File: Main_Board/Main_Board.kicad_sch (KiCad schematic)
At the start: 30 parts, among them J1 RJ45_LED_Shielded, SW1 SW_SPDT, SW2 SW_Push, SW3 SW_Push, SW4 SW_Push, SW5 SW_Push, SW6 SW_Push, SW7 SW_Push, SW8 SW_Push, SW9 SW_Push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

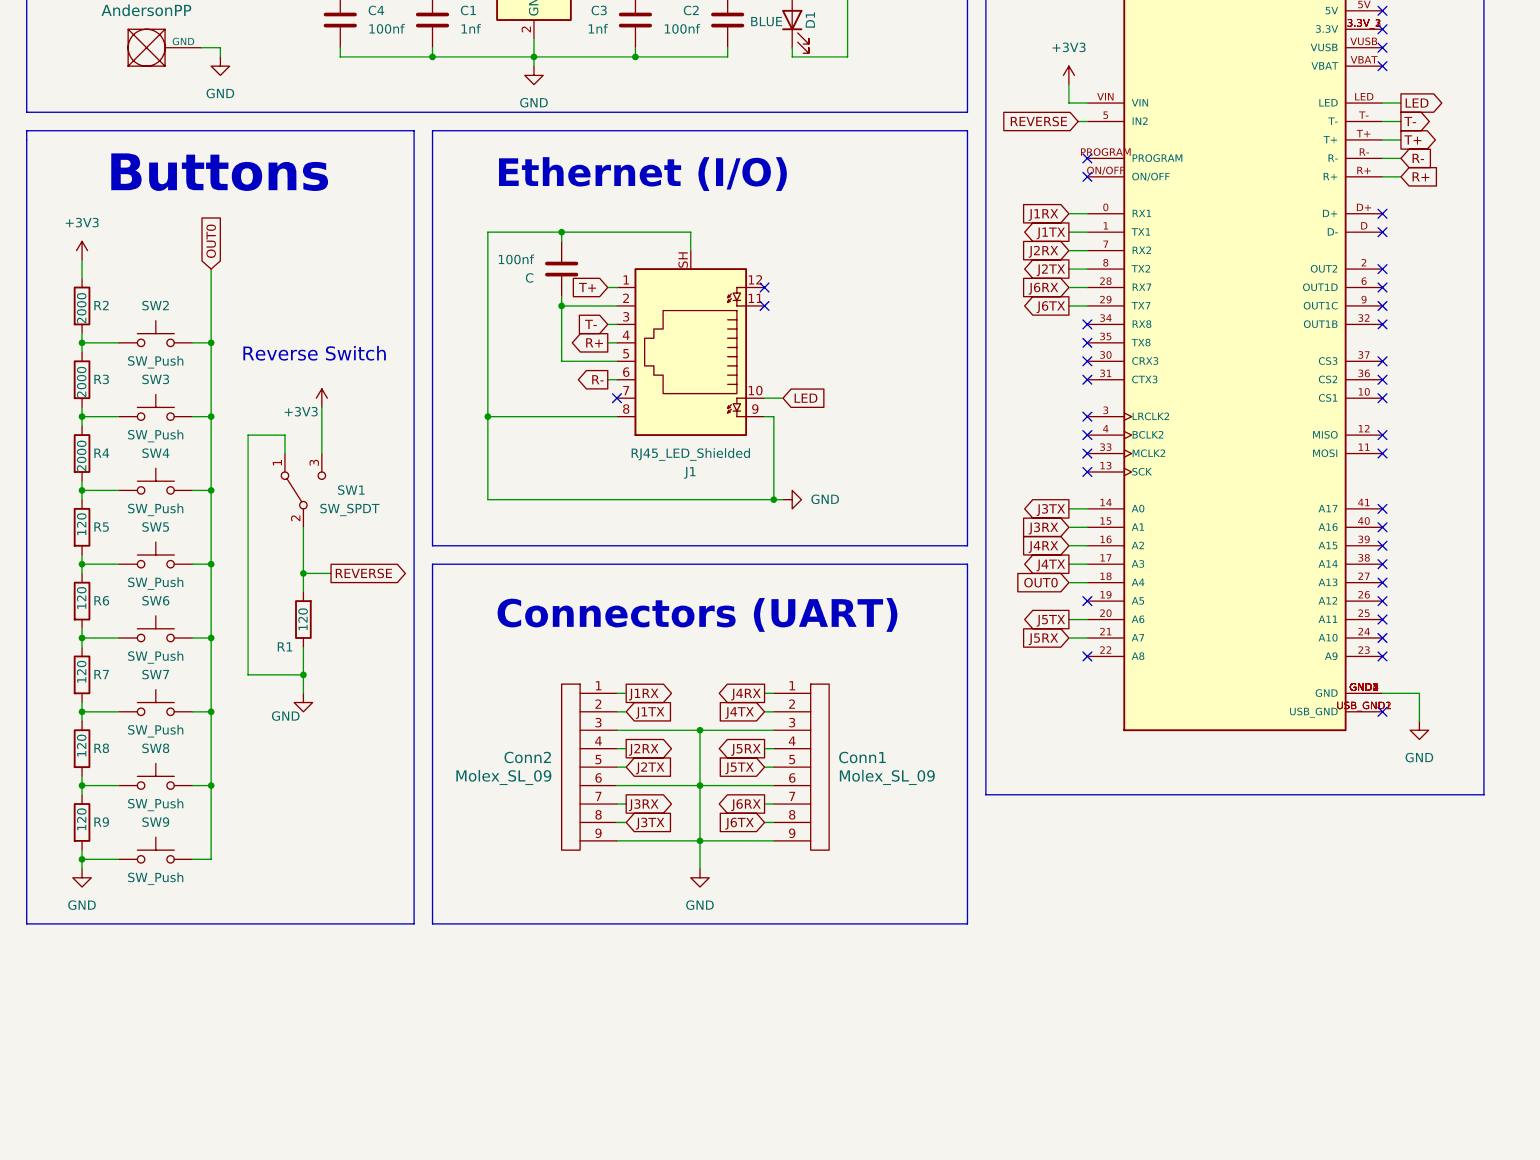
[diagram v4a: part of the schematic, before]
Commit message: Added Keyboard Matrix Layout
Added a keyboard circuit layout so any button can be pressed at the same time and programmed to work like a keyboard.
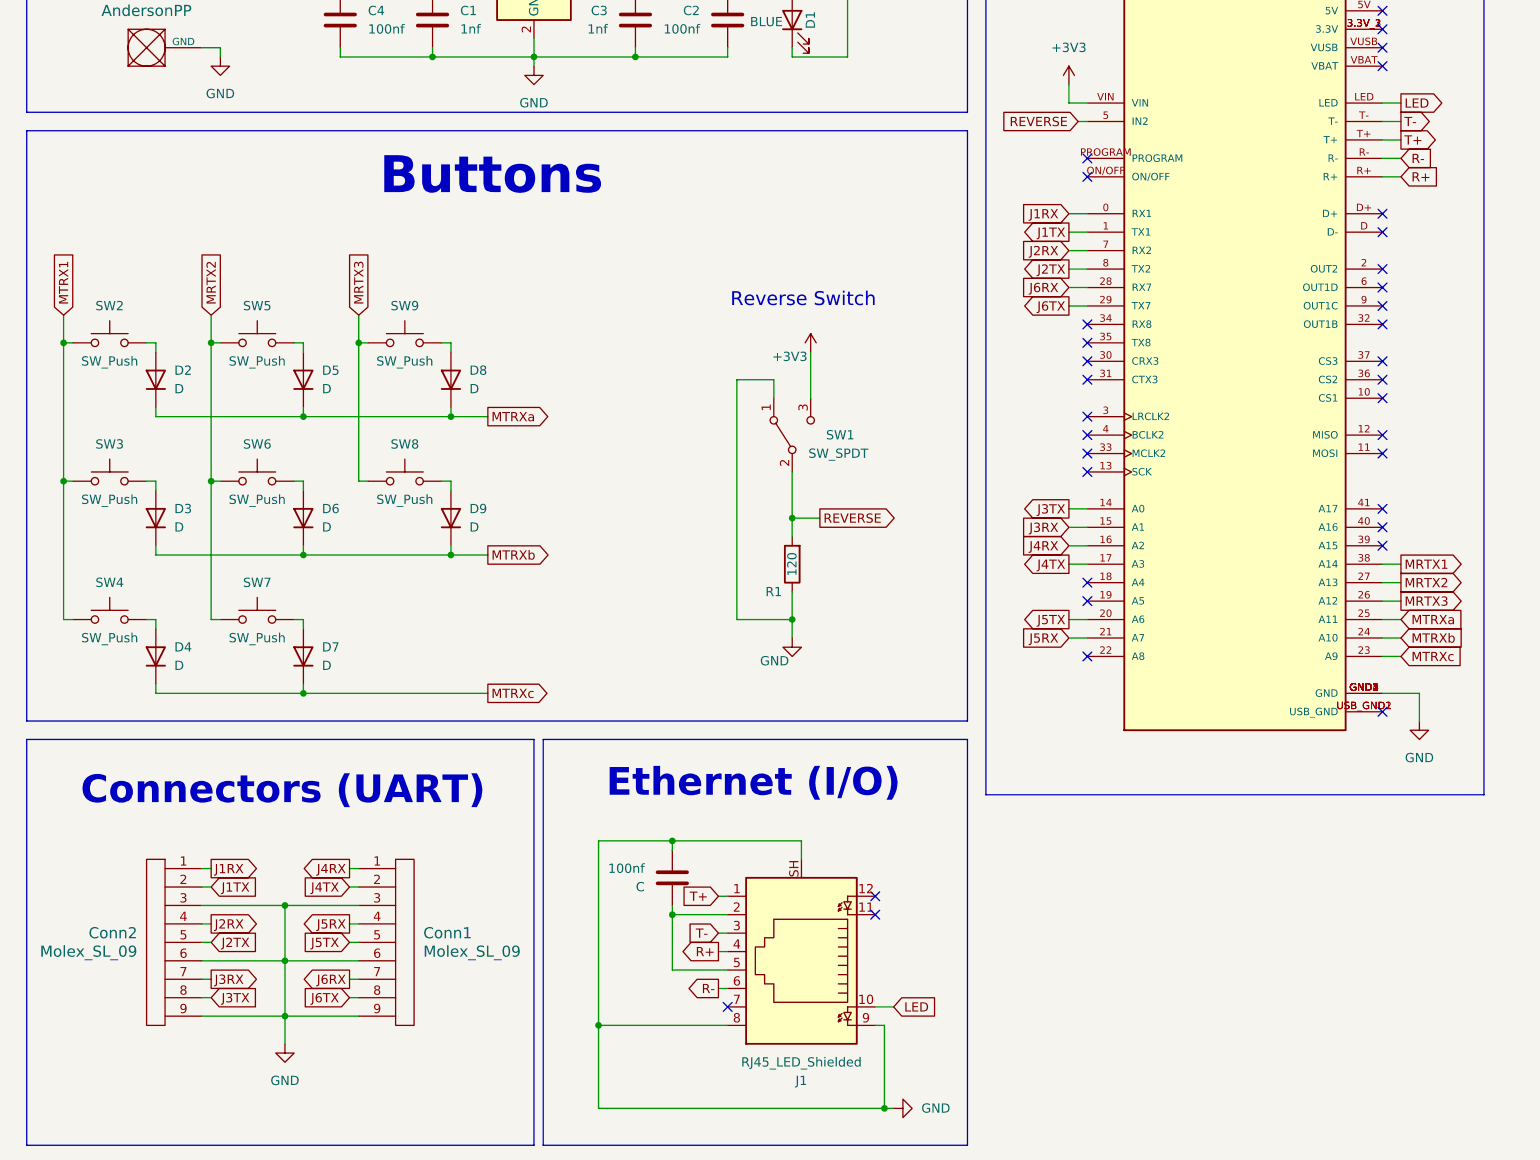
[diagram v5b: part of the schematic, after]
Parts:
- removed R2, R3, R4: 2000, symbol Device:R
- removed R5, R6, R7, R8, R9: 120, symbol Device:R
- added D2, D3, D4, D5, D6, D7, D8, D9: D, symbol Device:D
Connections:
- net GND: no longer SW9.1
- net MRTX2: now reaches SW7.1
- net MRTX2: now also SW5.1, SW6.1, U2.27 (A13)
- net MRTX3: now reaches SW8.1
- net MRTX3: now also SW9.1, U2.26 (A12)
- net MTRX1: now reaches SW4.1
- net MTRX1: now also SW2.1, SW3.1
- net MTRXc: now reaches U2.23 (A9)
- net MTRXc: now also D4.1 (K), D7.1 (K)
- net MTRXb: now reaches U2.24 (A10)
- net MTRXb: now also D3.1 (K), D6.1 (K), D9.1 (K)
- net MTRXa: now reaches U2.25 (A11)
- net MTRXa: now also D2.1 (K), D5.1 (K), D8.1 (K)
- net MRTX1: now reaches U2.38 (A14)
- removed net OUT0: SW2.2, SW3.2, SW4.2, SW5.2, SW6.2, SW7.2, SW8.2, SW9.2, U2.18 (A4)
- new net: D4.2 (A), SW4.2
- new net: D7.2 (A), SW7.2
- new net: D8.2 (A), SW9.2
- new net: D5.2 (A), SW5.2
- new net: D3.2 (A), SW3.2
- new net: D2.2 (A), SW2.2
- new net: D9.2 (A), SW8.2
- new net: D6.2 (A), SW6.2
- no-connect marks 40 -> 35
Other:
- moved on the sheet: 100nf, Conn1, Conn2, J1, R1, SW1, SW2, SW3, SW4, SW5, SW6, SW7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
